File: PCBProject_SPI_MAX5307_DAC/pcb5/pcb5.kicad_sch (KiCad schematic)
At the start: 80 parts, among them IC1 MAX5725BAUP+, U1 SN74HC365D, U2 LM224DR, U3 LM224DR

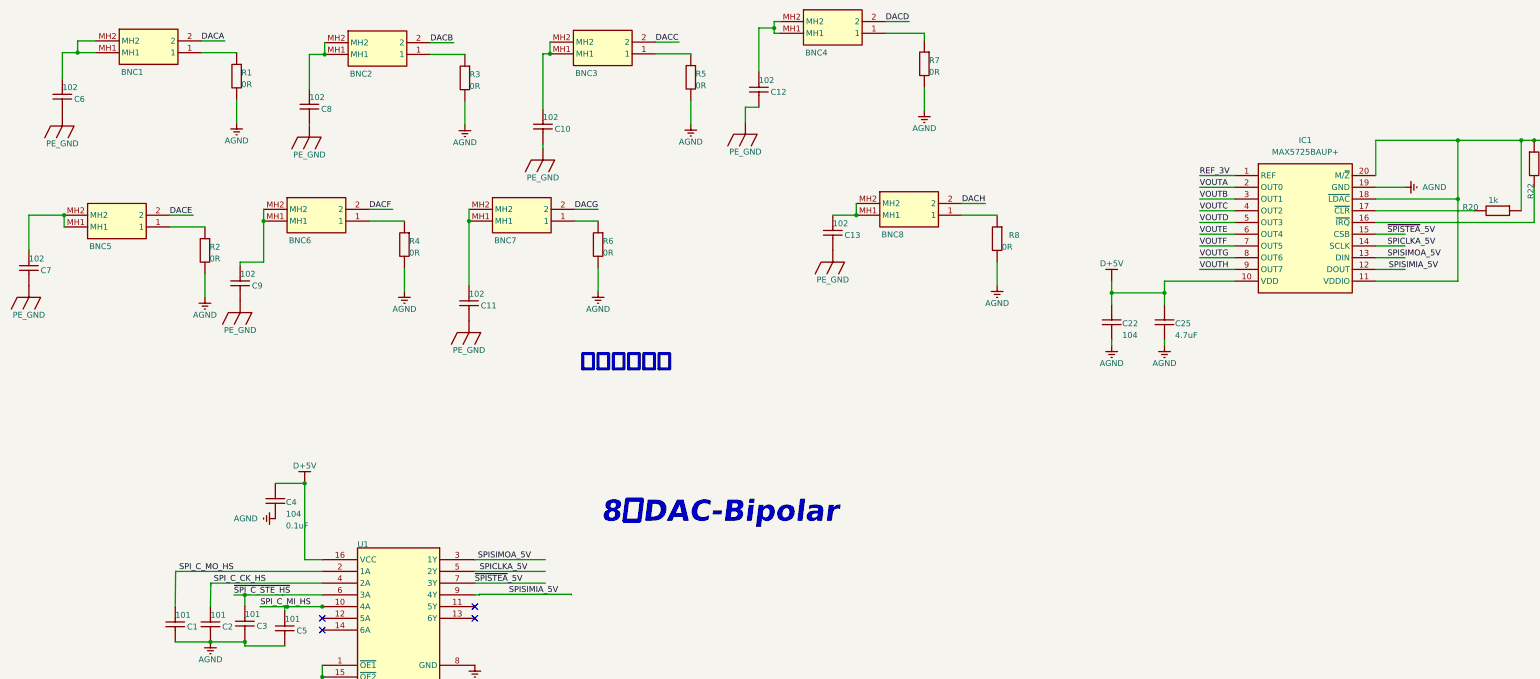
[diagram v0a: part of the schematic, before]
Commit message: fix VDD and ref_3V, DC_bus location
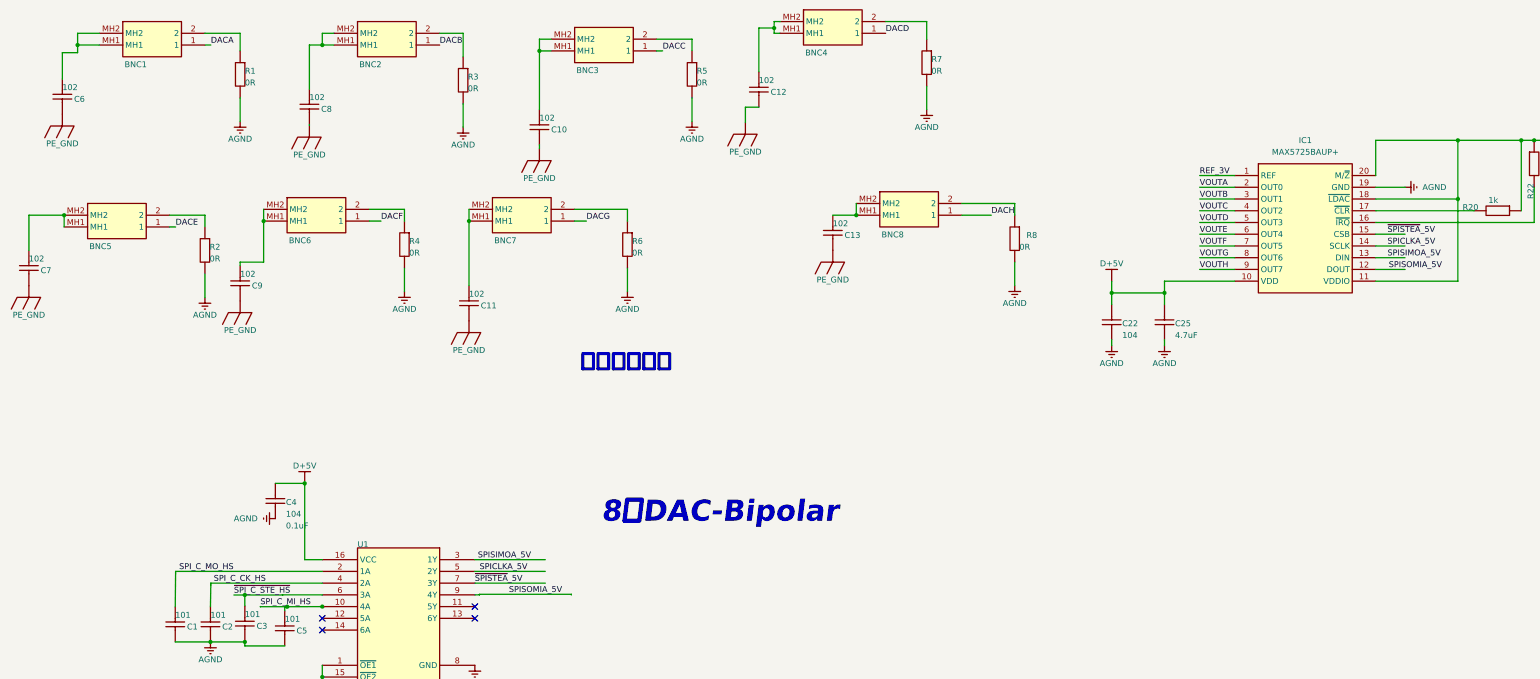
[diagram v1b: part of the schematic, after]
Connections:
- net DACA: now also BNC1.1; no longer BNC1.2
- net DACB: now also BNC2.1; no longer BNC2.2
- net DACC: now also BNC3.1; no longer BNC3.2
- net DACD: now also BNC4.1; no longer BNC4.2
- net DACE: now also BNC5.1; no longer BNC5.2
- net DACF: now also BNC6.1; no longer BNC6.2
- net DACG: now also BNC7.1; no longer BNC7.2
- net DACH: now also BNC8.1; no longer BNC8.2
- net at R6.2: now also BNC7.2; no longer BNC7.1
- net at R3.2: now also BNC2.2; no longer BNC2.1
- net at R8.2: now also BNC8.2; no longer BNC8.1
- net at R7.2: now also BNC4.2; no longer BNC4.1
- net at R1.2: now also BNC1.2; no longer BNC1.1
- net at R5.2: now also BNC3.2; no longer BNC3.1
- net at R2.2: now also BNC5.2; no longer BNC5.1
- net at R4.2: now also BNC6.2; no longer BNC6.1
- net SPISIMIA_5V renamed SPISOMIA_5V
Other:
- moved on the sheet: BNC1, BNC2, BNC3, C10, R1, R3, R5, R6, R7, R8

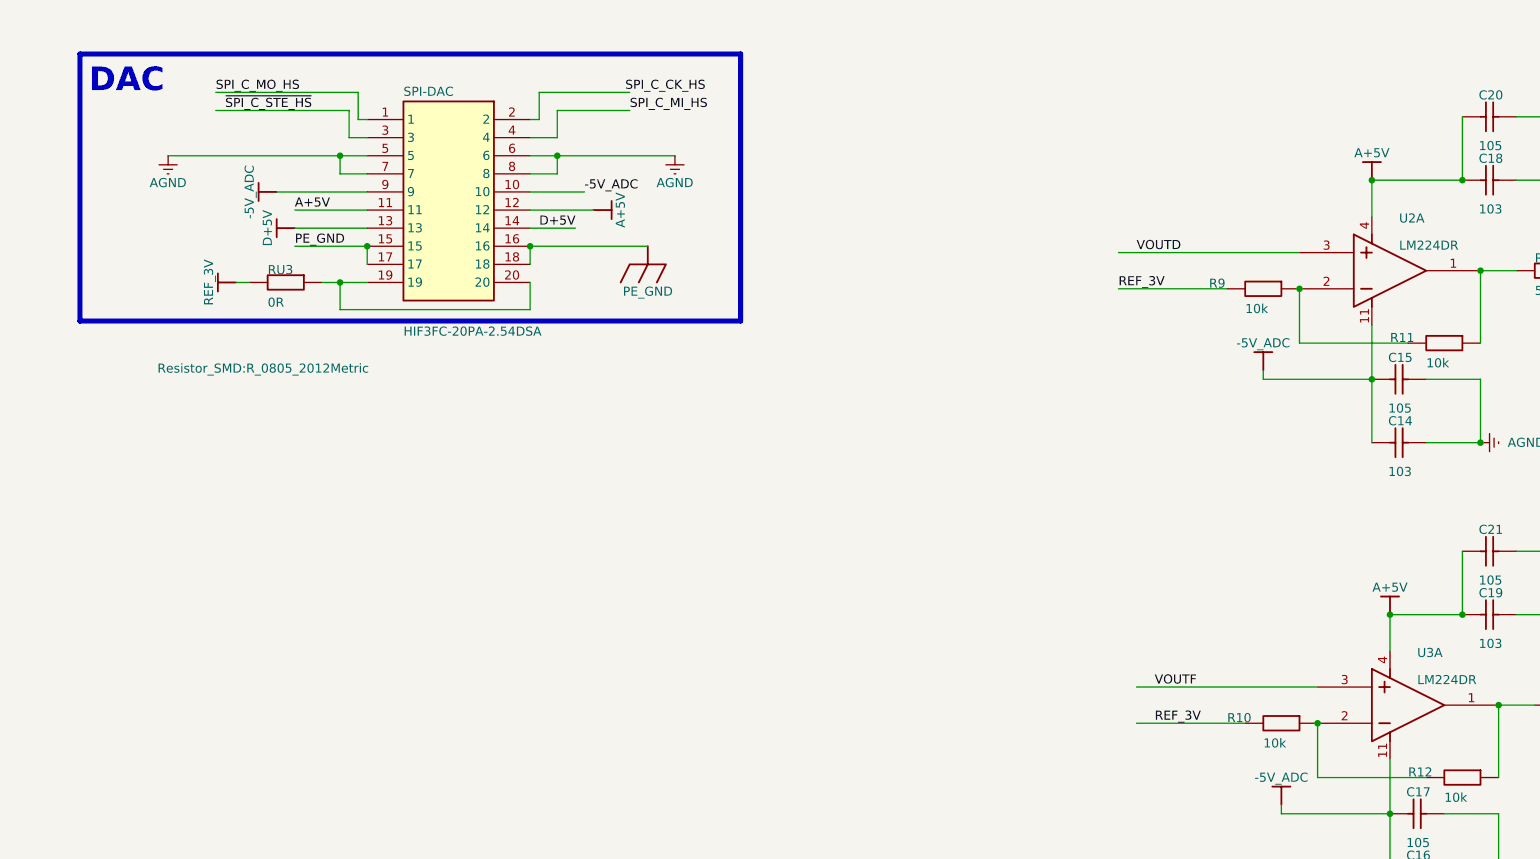
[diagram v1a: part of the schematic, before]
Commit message: 修改DAC接口定义
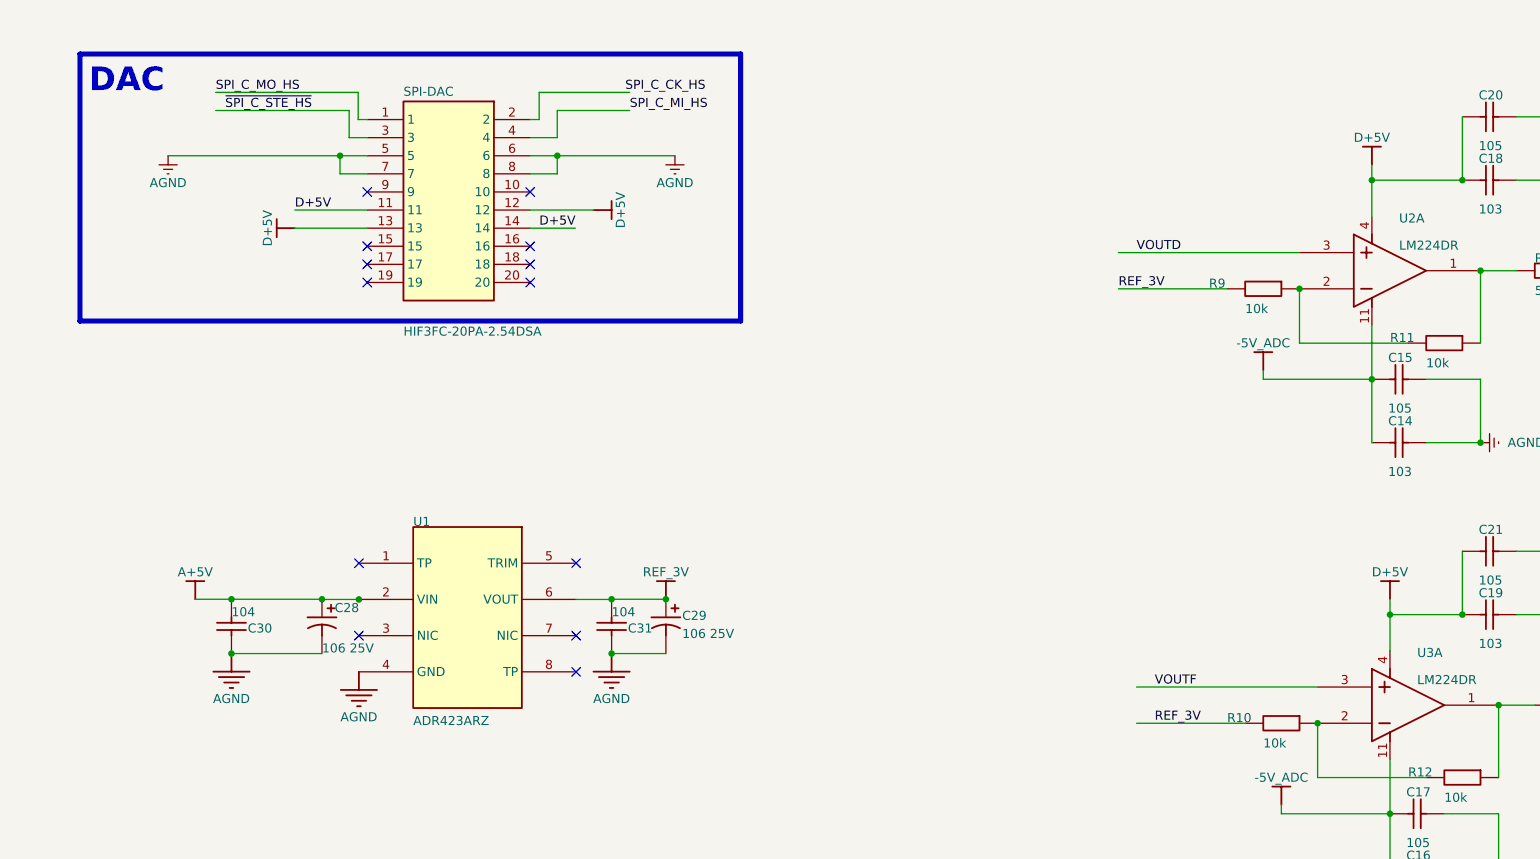
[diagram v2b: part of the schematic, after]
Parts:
- removed RU3: 0R, Resistor_SMD:R_0805_2012Metric, symbol sheet1-altium-import:root_0_Res2
- added C28, C29: 106 25V, Oshinoko:1206 (钽电容), symbol SensorLEM-altium-import:root_3_Cap Pol3
- added C30, C31: 104, Capacitor_SMD:C_0805_2012Metric, symbol SensorLEM-altium-import:root_1_Cap Semi
- added U1: ADR423ARZ, Oshinoko:SOIC-8, symbol SensorLEM-altium-import:root_0_ADR423ARZ
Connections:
- net -5V_ADC: no longer SPI-DAC.10, SPI-DAC.9
- net A+5V: now also C28.1, C30.2, U1.2 (VIN); no longer C18.1, C19.1, C20.2, C21.2, SPI-DAC.11, SPI-DAC.12, U2.4, U3.4
- net D+5V: now also C18.1, C19.1, C20.2, C21.2, SPI-DAC.11, SPI-DAC.12, U2.4, U3.4
- net PE_GND: no longer SPI-DAC.15, SPI-DAC.16, SPI-DAC.17, SPI-DAC.18
- net REF_3V: now also C29.1, C31.2, U1.6 (VOUT)
- net at SPI-DAC.19: no longer SPI-DAC.20
- new net AGND: C28.2, C29.2, C30.1, C31.1, U1.4 (GND)
- no-connect marks 4 -> 17

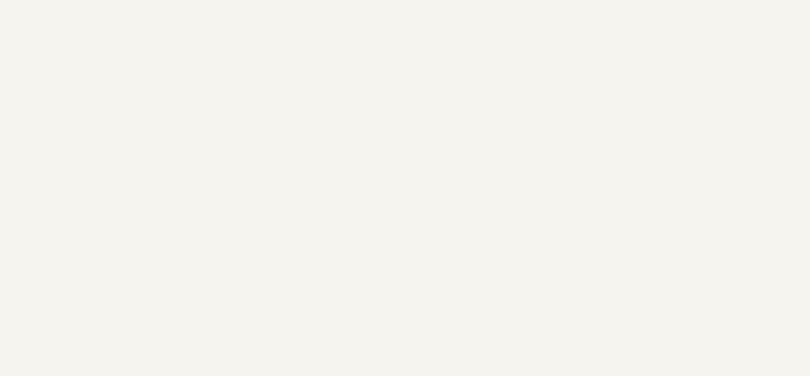
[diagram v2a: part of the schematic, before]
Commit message: 重定义了DAC接口和修复了底板的PWM的bug，还需实现DAC电源集成
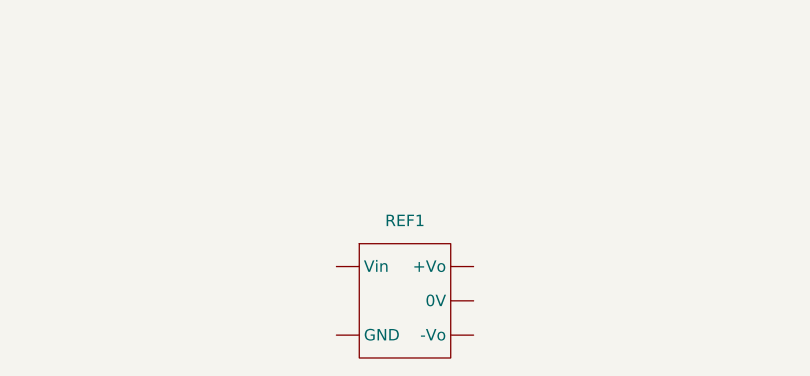
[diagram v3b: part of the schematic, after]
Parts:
- added REF1: ~, E_S-2WR3:E_S-2WR3, symbol 1mmlab:E0505S-2WR3
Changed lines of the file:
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@@
+    )
+  )
+  (symbol (lib_id "1mmlab:E0505S-2WR3") (at 81.28 332.74 0) (unit 1)
+    (in_bom yes) (on_board yes) (dnp no) (fields_autoplaced)
+    (property "Reference" "REF1" (at 83.82 330.2 0)
+      (effects (font (size 1.27 1.27)))
+    )
+    (property "Value" "~" (at 81.28 332.74 0)
+      (effects (font (size 1.27 1.27)))
+    )
+    (property "Footprint" "E_S-2WR3:E_S-2WR3" (at 81.28 328.93 0)
+      (effects (font (size 1.27 1.27)) hide)
+    )
+    (property "Datasheet" "" (at 81.28 332.74 0)
+      (effects (font (size 1.27 1.27)) hide)
+    )
+    (pin "")
+    (pin "")
+    (pin "")
+    (pin "")
+    (pin "")
+    (instances
+      (project "pcb5"
+        (path "/c9979d34-4f34-40f0-9fff-955f110a3714"
+          (reference "REF1") (unit 1)
+        )
+      )
     )
   )

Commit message: DAC for 28388
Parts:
- removed REF1: ~, E_S-2WR3:E_S-2WR3, symbol 1mmlab:E0505S-2WR3
- added C37, C38: 10uF, Capacitor_SMD:C_0805_2012Metric, symbol SensorLEM-altium-import:root_1_Cap Semi
- added C39: 0.1uF, Capacitor_SMD:C_0805_2012Metric, symbol SensorLEM-altium-import:root_1_Cap Semi
- added U5: LM2662M_NOPB, SamacSys_Parts:SOIC127P600X175-8N, symbol LM2662M_NOPB:LM2662M_NOPB
- C34: renamed from C28; footprint Oshinoko:1206 (钽电容) -> Capacitor_SMD:C_1206_3216Metric
- C36: renamed from C29; footprint Oshinoko:1206 (钽电容) -> Capacitor_SMD:C_1206_3216Metric
- U4: renamed from U1; footprint Oshinoko:SOIC-8 -> SamacSys_Parts:SOIC127P600X175-8N
- renumbered C30 to C33, C31 to C35, SPI-DAC to SPI-DAC1
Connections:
- net A+5V is gone; now on net D+5V: C33.2, C34.1, U4.2 (VIN)
- net AGND is gone; now on net GNDREF: C33.1, C34.2, C35.1, C36.2, U4.4 (GND)
- net D+5V: now also U5.8 (V+)
- net GNDREF: now also C38.1, C39.1, U5.3 (GND), U5.6 (LV)
- net PE_GND: now also SPI-DAC1.17, SPI-DAC1.18, SPI-DAC1.19, SPI-DAC1.20
- net -5V_ADC renamed -5V
- net -5V: now also C38.2, C39.2, U5.5 (OUT)
- net SPI_C_CK_HS renamed SPI_CK_HS
- net SPI_C_MI_HS renamed SPI_MI_HS
- net SPI_C_MO_HS renamed SPI_MO_HS
- net ~{SPI_C_STE_HS} renamed ~{SPI_STE_HS}
- new net: C37.2, U5.2 (CAP+)
- new net: C37.1, U5.4 (CAP-)
- no-connect marks 17 -> 15
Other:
- moved on the sheet: BNC8, C13, C22, C25, R8
